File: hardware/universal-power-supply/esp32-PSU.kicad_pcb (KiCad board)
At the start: 2 copper layers, 45 x 40 mm, 12 parts, among them P1 CONN_01X02, P101 EXT_HEADER, P2 EXT_HEADER, U1 WPMDL110

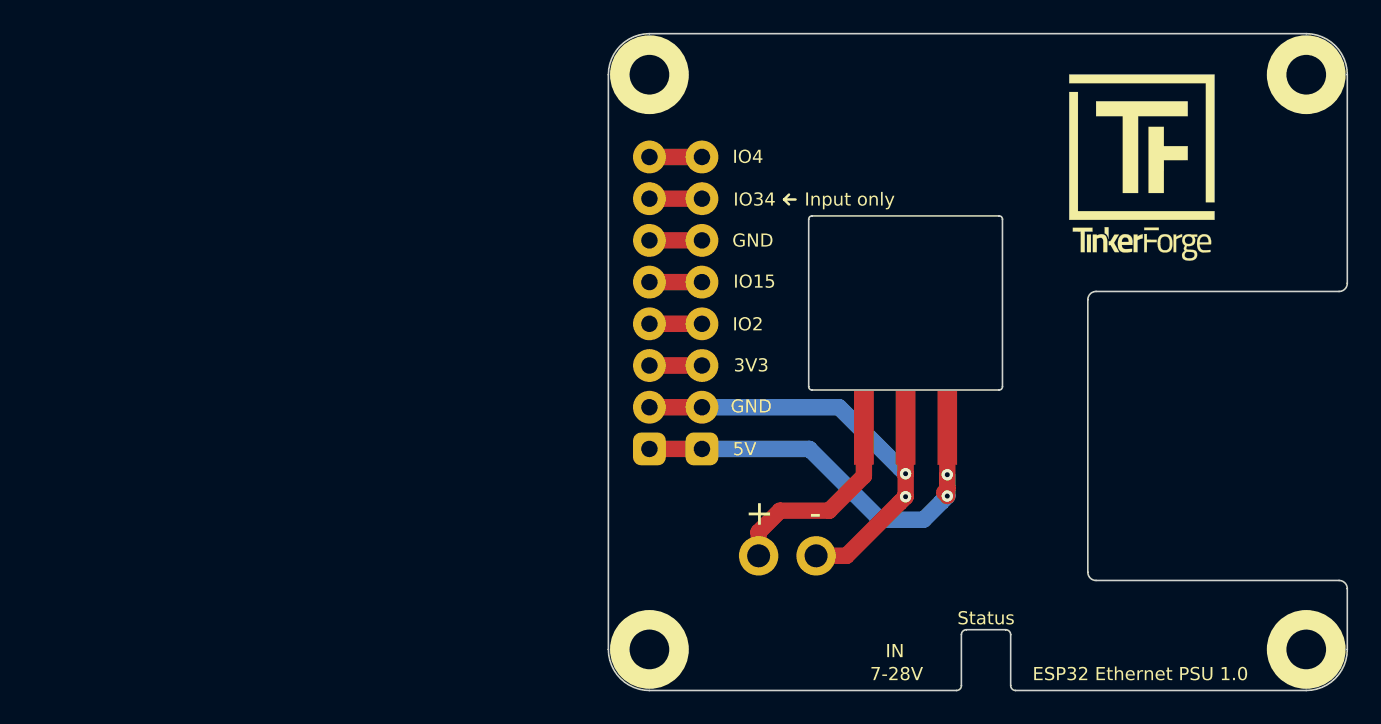
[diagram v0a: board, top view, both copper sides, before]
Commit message: added universal esp32 psu
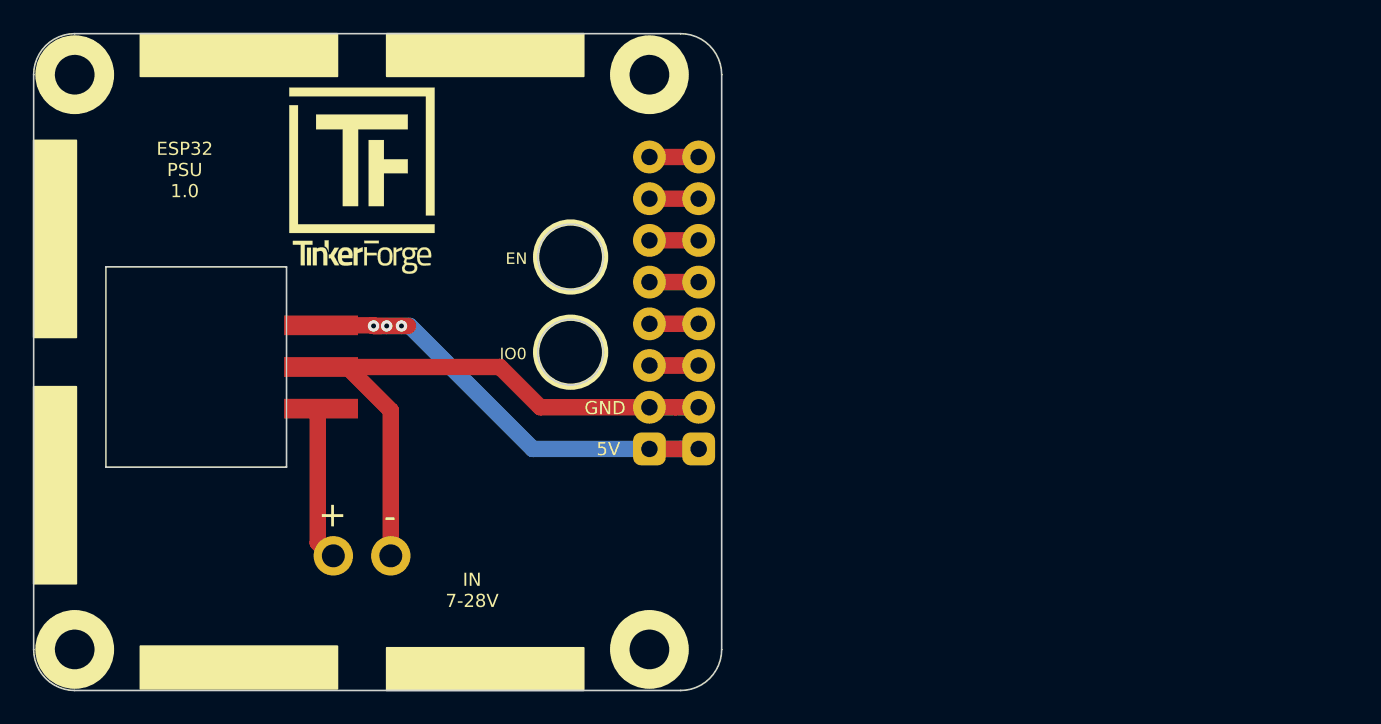
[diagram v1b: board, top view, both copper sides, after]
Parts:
- removed F105, F106: DRILL, kicad-libraries:DRILL_NP
- added F101: DRILL, kicad-libraries:DRILL_NP, F.Cu at (116.3, 126.2)
- added F102: DRILL, kicad-libraries:DRILL_NP, F.Cu at (116.3, 161.2)
- moved G*** 47.5 mm to (133.8, 132.4)
- moved VAL 45.6 mm to (125.2, 132.4)
- moved G*** 45.2 mm to (133.8, 132.2)
- moved U1 39.4 mm to (127.5, 143.9), turned to 180 degrees
- moved P1 25.9 mm to (133.8, 155.4)
- moved VAL 22.4 mm to (141.9, 132.3)
- moved P2 0.20 mm to (154.3, 140.1)
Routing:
- net Net-(P1-Pad2): track 28.4 -> 41.2 mm, vias 2 -> 0
- net OUT_5V: track 26.0 -> 31.7 mm, vias 2 -> 3
- net IN_7-28V: track 12.2 -> 9.52 mm
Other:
- board size 45 x 40 mm -> 41.9 x 40 mm
- board text added: "A"
- board text added: "B"
- board text added: "C"
- board text added: "Copyright Tinkerforge GmbH 2021. This documentation describes Open Hardware and is licensed under the CERN OHL v. 1.1. You may redistribute and modify this documentation under the terms of the CERN OHL v.1.1. (http://ohwr.org/cernohl). This documentation is distributed WITHOUT ANY EXPRESS OR IMPLIED WARRANTY, INCLUDING OF MERCHANTABILITY, SATISFACTORY QUALITY AND FITNESS FOR A PARTICULAR PURPOSE.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"
- board text added: "D"
- board text added: "E"
- board text added: "EN"
- board text added: "ESP32 PSU 1.0"
- board text added: "F"
- board text added: "IN 7-28V"
- board text added: "IO0"
- board text removed: "3V3"
- board text removed: "7-28V"
- board text removed: "ESP32 Ethernet PSU 1.0"
- board text removed: "IN"
- board text removed: "IO15"
- board text removed: "IO2"
- board text removed: "IO34"
- board text removed: "IO4"
- board text removed: "Input only"
- board text removed: "Status"
